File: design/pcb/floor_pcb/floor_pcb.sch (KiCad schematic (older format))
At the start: 11 parts, among them J1 Conn_01x10_Male, J10 shock_grid, J11 shock_grid, J2 Conn_01x10_Male, J3 DB25_Male, J4 shock_grid, J5 shock_grid, J6 shock_grid, J7 shock_grid, J8 shock_grid, J9 shock_grid

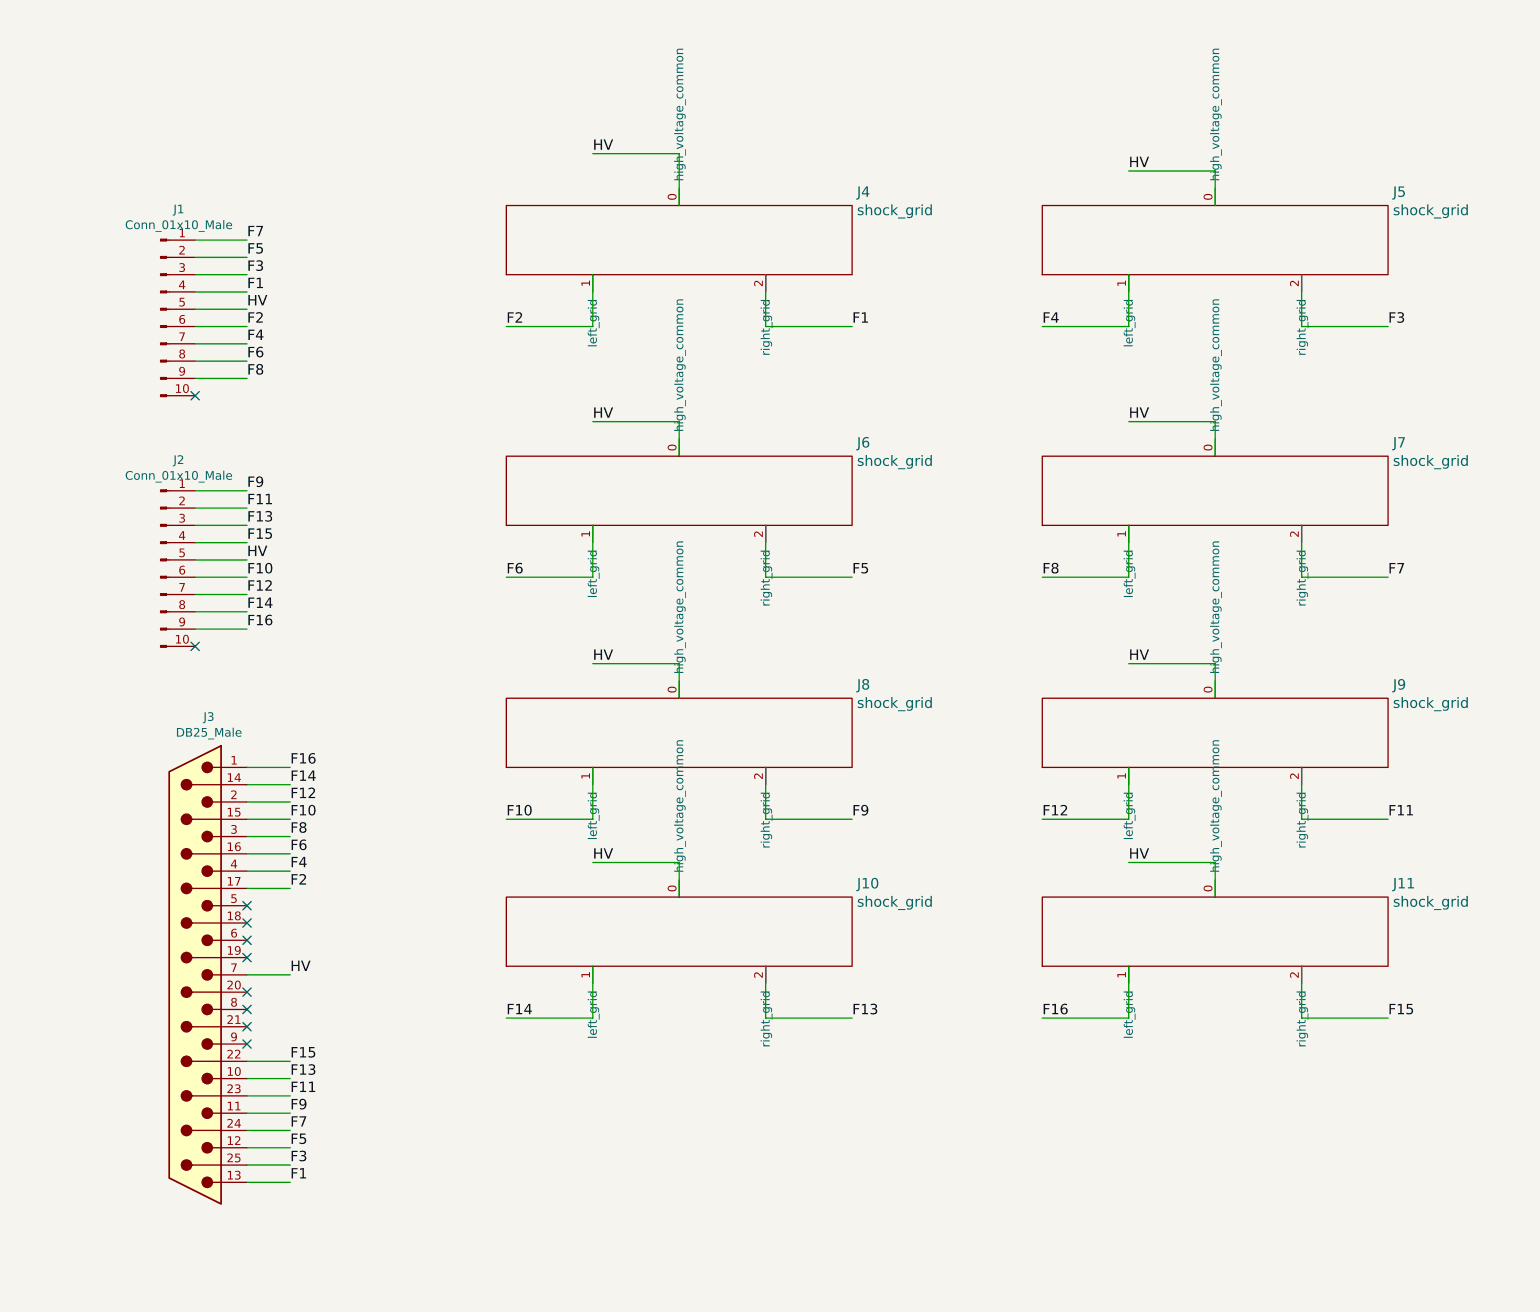
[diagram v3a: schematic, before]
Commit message: Seem to have make_board working to align top and bottom connectors, and J3 on the bottom, but I need to pick different offsets from nearest grid for top and bottom. May need to make ceiling board a little longer on the top. ADD EXTRA MOUNTING HOLES IN BOTTOM.
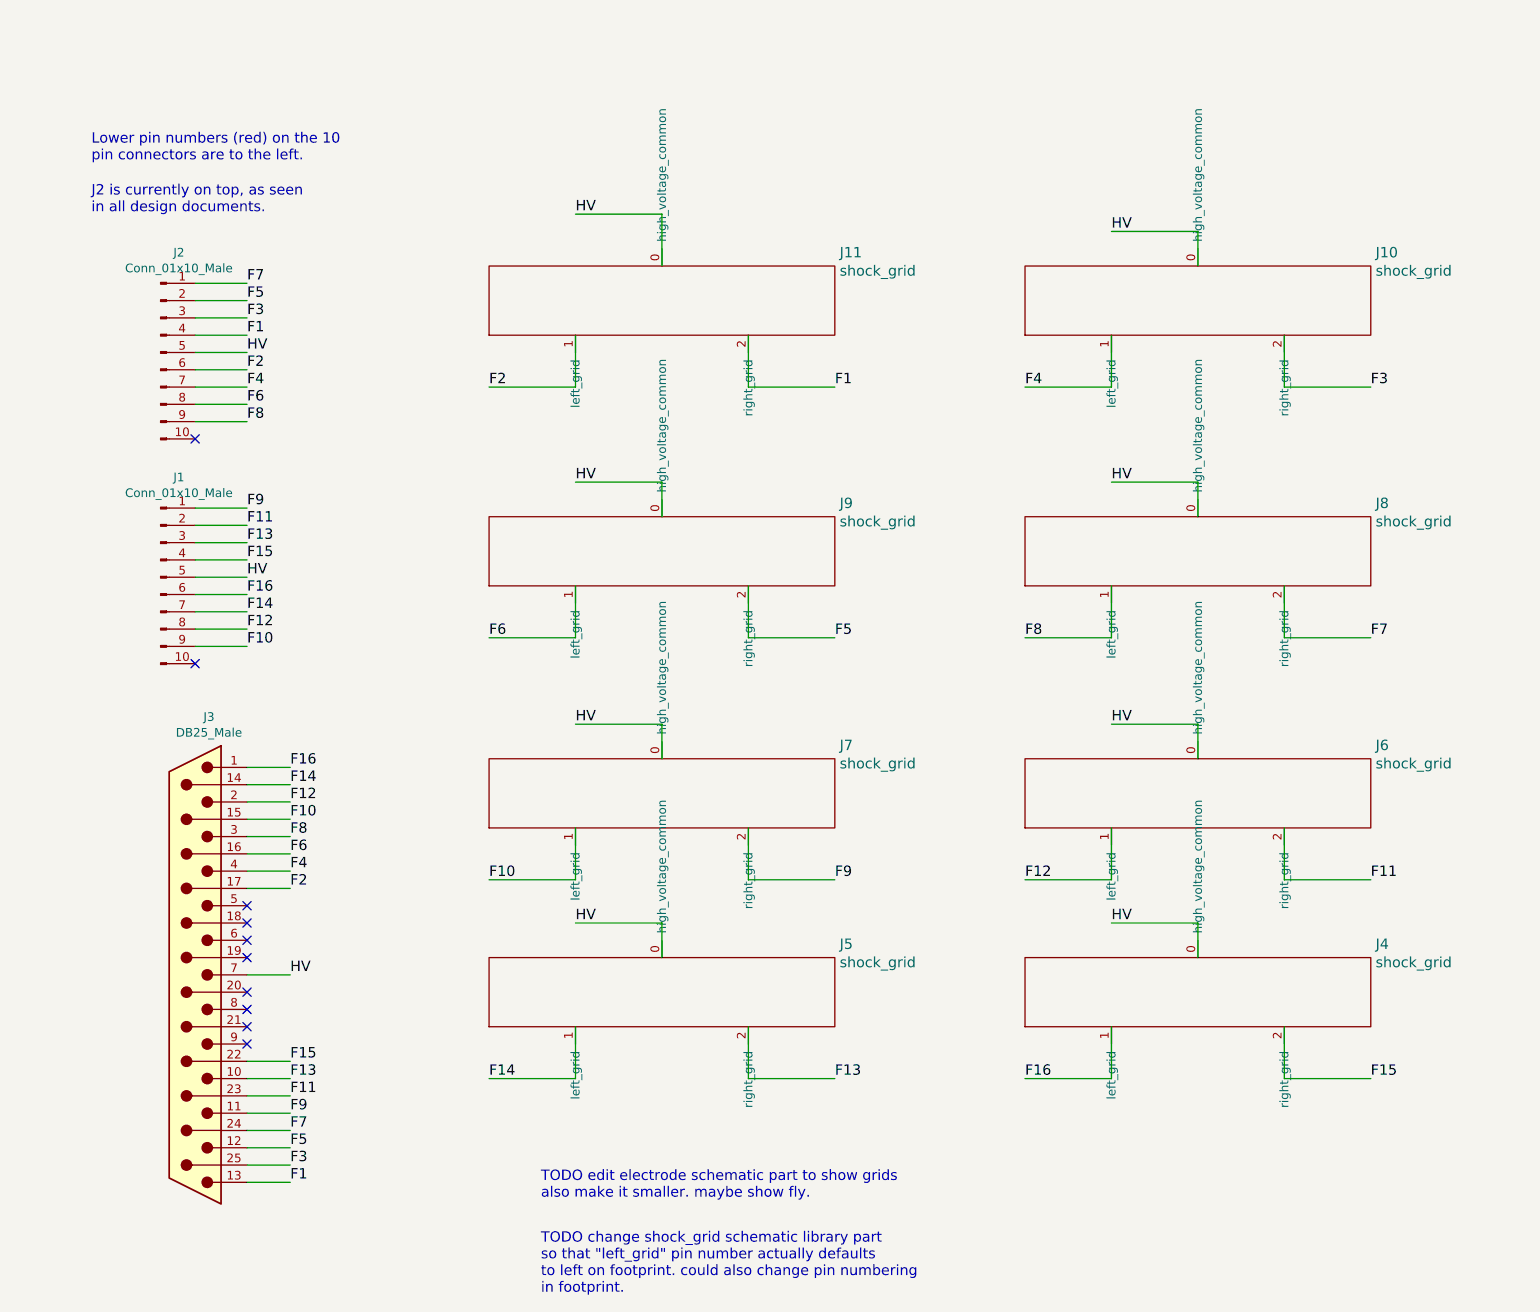
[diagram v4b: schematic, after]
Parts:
- renumbered J5 to J10, J4 to J11, J11 to J4, J10 to J5, J9 to J6, J8 to J7, J7 to J8, J6 to J9
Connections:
- net F1: now also J2.4 (Pin_4); no longer J1.4 (Pin_4)
- net F10: now also J1.9 (Pin_9); no longer J2.6 (Pin_6)
- net F11: now also J1.2 (Pin_2); no longer J2.2 (Pin_2)
- net F12: now also J1.8 (Pin_8); no longer J2.7 (Pin_7)
- net F13: now also J1.3 (Pin_3); no longer J2.3 (Pin_3)
- net F14: now also J1.7 (Pin_7); no longer J2.8 (Pin_8)
- net F15: now also J1.4 (Pin_4); no longer J2.4 (Pin_4)
- net F16: now also J1.6 (Pin_6); no longer J2.9 (Pin_9)
- net F2: now also J2.6 (Pin_6); no longer J1.6 (Pin_6)
- net F3: now also J2.3 (Pin_3); no longer J1.3 (Pin_3)
- net F4: now also J2.7 (Pin_7); no longer J1.7 (Pin_7)
- net F5: now also J2.2 (Pin_2); no longer J1.2 (Pin_2)
- net F6: now also J2.8 (Pin_8); no longer J1.8 (Pin_8)
- net F7: now also J2.1 (Pin_1); no longer J1.1 (Pin_1)
- net F8: now also J2.9 (Pin_9); no longer J1.9 (Pin_9)
- net F9: now also J1.1 (Pin_1); no longer J2.1 (Pin_1)
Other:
- note added: "J2 is currently on top, as seen\nin all design documents."
- note added: "Lower pin numbers (red) on the 10\npin connectors are to the left."
- note added: "TODO change shock_grid schematic library part\nso that "left_grid" pin number actually defaults\nto left on footprint. could also change pin numbering\nin footprint."
- note added: "TODO edit electrode schematic part to show grids\nalso make it smaller. maybe show fly."
- moved on the sheet: J1, J10, J11, J2, J4, J5, J6, J7, J8, J9

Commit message: Before another attempt fixing symbol libraries in floor_pcb
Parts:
- J10, J11, J4, J5, J6, J7, J8, J9: symbol shock_grid -> shock_electrodes:shock_grid
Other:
- note added: "TODO change shock_electrodes:shock_grid schematic library part\nso that "left_grid" pin number actually defaults\nto left on footprint. could also change pin numbering\nin footprint."
- note removed: "TODO change shock_grid schematic library part\nso that "left_grid" pin number actually defaults\nto left on footprint. could also change pin numbering\nin footprint."
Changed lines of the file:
@@
 EESchema Schematic File Version 3
+LIBS:shock_electrodes
+LIBS:floor_pcb
 LIBS:Connector
-LIBS:shock_grid
-LIBS:floor_pcb-cache
 EELAYER 26 0
 EELAYER END
@@
 $EndComp
 $Comp
-L shock_grid J11
+L shock_electrodes:shock_grid J11
 U 1 1 59F778B5
 P 4250 1800
@@
 $EndComp
 $Comp
-L shock_grid J9
+L shock_electrodes:shock_grid J9
 U 1 1 59F779C5
 P 4250 3250
@@
 $EndComp
 $Comp
-L shock_grid J10
+L shock_electrodes:shock_grid J10
 U 1 1 59F77CE3
 P 7350 1800
@@
 $EndComp
 $Comp
-L shock_grid J8
+L shock_electrodes:shock_grid J8
 U 1 1 59F77DC7
 P 7350 3250
@@
 $EndComp
 $Comp
-L shock_grid J7
+L shock_electrodes:shock_grid J7
 U 1 1 59F77FF1
 P 4250 4650
@@
 $EndComp
 $Comp
-L shock_grid J6
+L shock_electrodes:shock_grid J6
 U 1 1 59F780F5
 P 7350 4650
@@
 $EndComp
 $Comp
-L shock_grid J5
+L shock_electrodes:shock_grid J5
 U 1 1 59F78242
 P 4250 5800
@@
 $EndComp
 $Comp
-L shock_grid J4
+L shock_electrodes:shock_grid J4
 U 1 1 59F7866D
 P 7350 5800
@@
 J2 is currently on top, as seen\nin all design documents.
 Text Notes 3550 7550 0    60   ~ 0
-TODO change shock_grid schematic library part\nso that "left_grid" pin number actually defaults\nto left on footprint. could also change pin numbering\nin footprint.
+TODO change shock_electrodes:shock_grid schematic library part\nso that "left_grid" pin number actually defaults\nto left on footprint. could also change pin numbering\nin footprint.
 Text Notes 3550 7000 0    60   ~ 0
 TODO edit electrode schematic part to show grids\nalso make it smaller. maybe show fly.

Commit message: After trying to make the (was file format 3) floor .sch more like shield .sch. May need to undo this, run through wizard to get in file format 4, then reapply changes.
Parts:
- J1, J2: symbol Conn_01x10_Male -> floor_pcb:Conn_01x10_Male
- J3: symbol DB25_Male -> floor_pcb:DB25_Male
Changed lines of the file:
@@
-EESchema Schematic File Version 3
+EESchema Schematic File Version 4
 LIBS:shock_electrodes
 LIBS:floor_pcb
@@
 $EndDescr
 $Comp
-L Conn_01x10_Male J2
+L floor_pcb:Conn_01x10_Male J2
 U 1 1 59F76DF3
 P 1350 2100
@@
 $EndComp
 $Comp
-L Conn_01x10_Male J1
+L floor_pcb:Conn_01x10_Male J1
 U 1 1 59F76D5B
 P 1350 3400
@@
 $EndComp
 $Comp
-L DB25_Male J3
+L floor_pcb:DB25_Male J3
 U 1 1 5A2622A3
 P 1550 5700
